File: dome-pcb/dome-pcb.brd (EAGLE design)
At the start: 45 x 73 mm, 15 parts, among them K1 CQ1-12V, K5 CQ1-12V, Q2 200mA/40V, Q4 200mA/40V

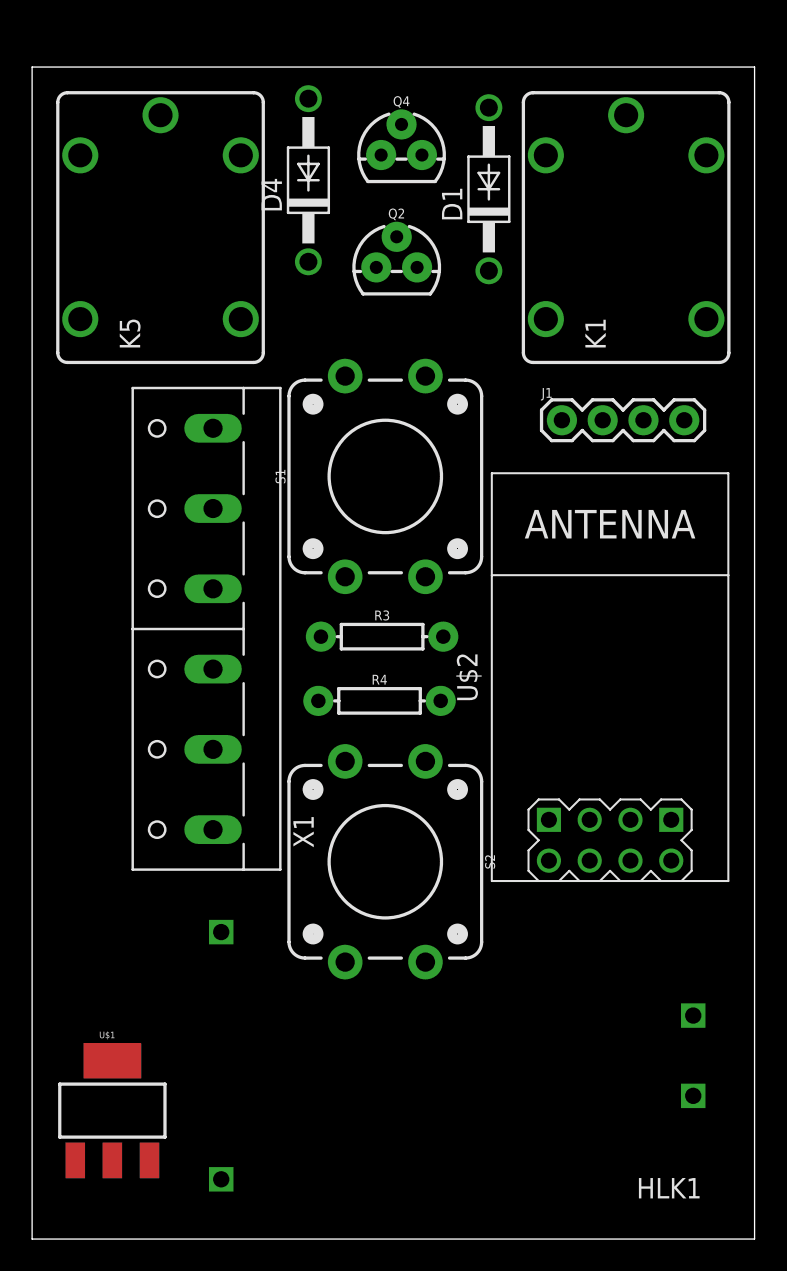
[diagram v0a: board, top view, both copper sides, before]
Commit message: Update PCB design with SMD components and a better layout
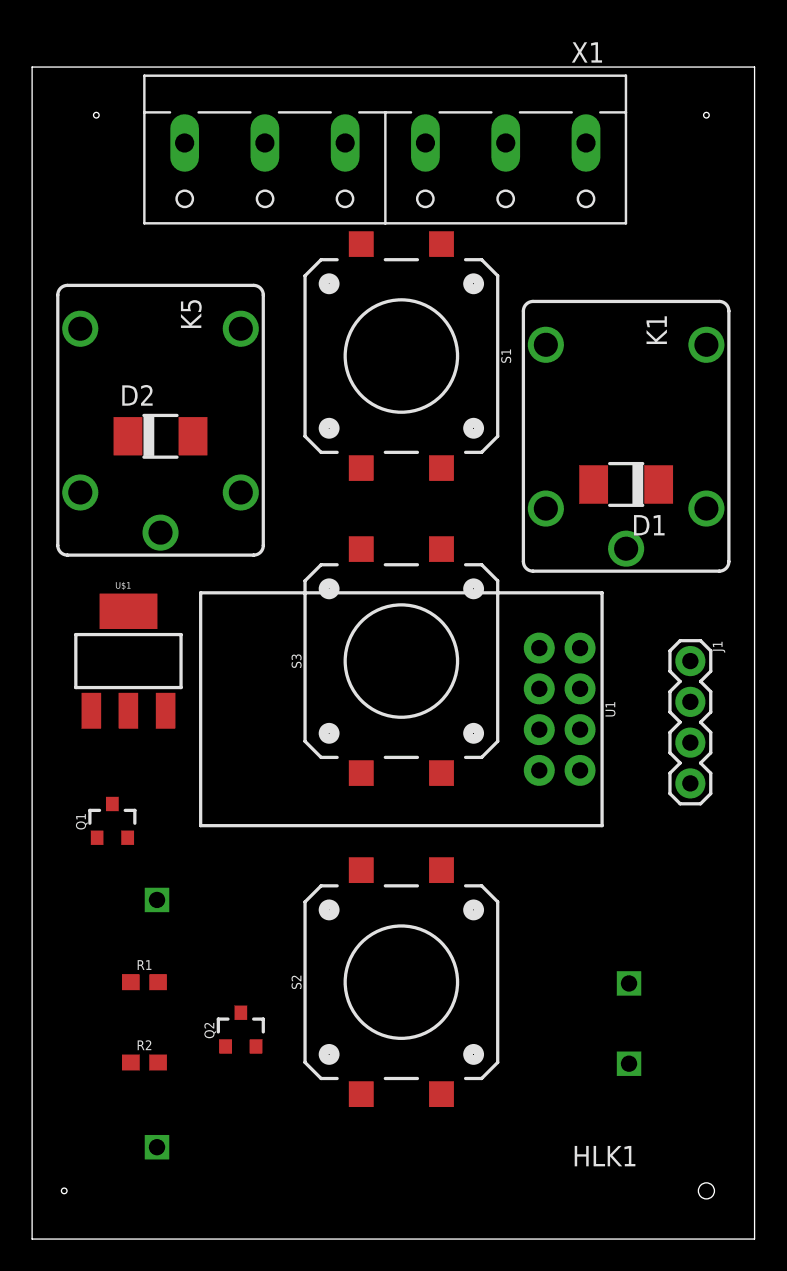
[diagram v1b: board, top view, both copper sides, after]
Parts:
- removed D4: 1N4004, diode:DO41-10
- removed Q4: 200mA/40V, DiscreteSemi:TO-92
- removed R3, R4: 10k, Resistors:AXIAL-0.3
- removed U$2: WIRELESS-WIFI-ESP-01, diy-modules:WIRELESS-WIFI-ESP-01
- added D2: (no value), diode:DO-214AC
- added Q1: 500mA/300V, DiscreteSemi:SOT23-3
- added R1, R2: 10k, Resistors:0603
- added S3: MOMENTARY-SWITCH-SPST-SMD-12MM, Switches:TACTILE_SWITCH_SMD_12MM
- added U1: ESP8266_ESP-01, RF:ESP8266_ESP-01
- D1: value 1N4004 -> (none); device diode:DO41-10 -> diode:DO-214AC
- Q2: value 200mA/40V -> 500mA/300V; device DiscreteSemi:TO-92 -> DiscreteSemi:SOT23-3
- S1, S2: value MOMENTARY-SWITCH-SPST-PTH-12MM -> MOMENTARY-SWITCH-SPST-SMD-12MM; device Switches:TACTILE_SWITCH_PTH_12MM -> Switches:TACTILE_SWITCH_SMD_12MM
- moved Q2 48.5 mm to (13.0, 13.0)
- moved X1 31.4 mm to (22.0, 67.0), turned to 180 degrees
- moved U$1 28.0 mm to (6.00, 36.0)
- moved D1 20.3 mm to (37.0, 47.0), turned to 180 degrees
- moved J1 17.0 mm to (41.0, 36.0), turned to 270 degrees
- moved K1 13.0 mm to (37.0, 50.0), turned to 270 degrees
- moved K5 12.0 mm to (8.00, 51.0), turned to 270 degrees
- moved S1 7.57 mm to (23.0, 55.0), turned to 270 degrees
- moved S2 7.57 mm to (23.0, 16.0), turned to 90 degrees
- moved HLK1 4.47 mm to (22.5, 13.4)
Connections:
- removed net VCC: U$2.D2
- new net N$3: S3.3
- net 5V: now also D2.C; no longer D4.C
- net GND: now also Q1.2, S3.1; no longer Q2.1, Q4.1, U$2.A1
- net N$10: now also R2.2; no longer Q2.2, R3.P$2
- net N$11: now also D1.A, Q1.3; no longer D4.A, Q4.3
- net N$12: now also Q1.1, R1.2; no longer Q4.2, R4.P$2
- net N$9: now also D2.A; no longer D1.A, Q2.3

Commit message: PCB Schematics and board
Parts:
- removed Q1, Q2: 500mA/300V, DiscreteSemi:SOT23-3
- added C1, C2: 10uF, Capacitors:0603
- added Q3, Q4: 600mA/40V, DiscreteSemi:SOT23-3
- added R3: 10k, Resistors:0603
- added S4, S5: (no value), Switches:TACTILE_SWITCH_SMD_5.2MM
- moved R1 43.3 mm to (32.5, 51.0), turned to 90 degrees
- moved R2 41.2 mm to (3.00, 52.0), turned to 90 degrees
- moved J1 7.07 mm to (40.0, 29.0), turned to 90 degrees
- moved S2 4.03 mm to (22.5, 20.0)
- moved S1 2.06 mm to (22.5, 53.0)
- moved D1 1.58 mm to (37.5, 48.5), turned to 0 degrees
- moved X1 1.12 mm to (22.5, 66.0)
- moved K1 1.00 mm to (37.0, 51.0)
- moved K5 1.00 mm to (8.00, 52.0)
- moved U$1 1.00 mm to (5.00, 36.0)
- moved S3 0.71 mm to (22.5, 36.5)
- moved D2 0.50 mm to (8.00, 50.5)
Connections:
- removed net N$1: S1.3
- removed net N$2: S2.3
- removed net N$3: S3.3
- new net 3.3V: C2.1, J1.4, R3.2, U$1.2, U1.2, U1.4
- new net AC1: HLK1.P$1, X1.3
- new net AC2: HLK1.P$2, X1.4
- new net AC_SWITCH_1A: K1.NO, X1.1
- new net AC_SWITCH_1B: K1.C, X1.2
- new net AC_SWITCH_2A: K5.NO, X1.5
- new net AC_SWITCH_2B: K5.C, X1.6
- new net GPIO0: S3.3, S5.3, U1.6
- new net GPIO1: J1.3, S1.3, S2.3, U1.1
- new net GPIO2: R1.1, U1.7
- new net GPIO3: J1.2, R2.1, U1.5
- new net RST: R3.1, S4.3, S4.4, U1.3
- net 5V: now also C1.1, HLK1.P$4, K1.1, U$1.3
- net GND: now also C1.2, C2.2, HLK1.P$3, J1.1, Q3.2, Q4.2, S4.1, S4.2, S5.1, S5.2, U$1.1, U1.8; no longer Q1.2
- net N$10: now also Q4.1
- net N$11: now also Q3.3; no longer Q1.3
- net N$12: now also Q3.1; no longer Q1.1
- net N$9: now also K1.2, Q4.3
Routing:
- net GND: track 0.00 -> 220.7 mm, vias 0 -> 2
- net 5V: track 0.00 -> 108.7 mm
- net GPIO0: track 0.00 -> 90.7 mm, vias 0 -> 1
- net 3.3V: track 0.00 -> 72.6 mm
- net AC1: track 0.00 -> 65.5 mm
- net GPIO3: track 0.00 -> 64.8 mm, vias 0 -> 1
- net AC2: track 0.00 -> 58.5 mm
- net N$9: track 0.00 -> 47.7 mm
- net GPIO1: track 0.00 -> 44.7 mm
- net RST: track 0.00 -> 44.3 mm
- net N$11: track 0.00 -> 34.5 mm
- net AC_SWITCH_1B: track 0.00 -> 26.2 mm
- net AC_SWITCH_2B: track 0.00 -> 23.1 mm
- net GPIO2: track 0.00 -> 20.7 mm
- net AC_SWITCH_1A: track 0.00 -> 16.3 mm
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- added copper zone on layer 1, net GND
- added copper zone on layer 16, net GND
